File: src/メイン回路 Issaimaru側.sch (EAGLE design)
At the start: 3 parts

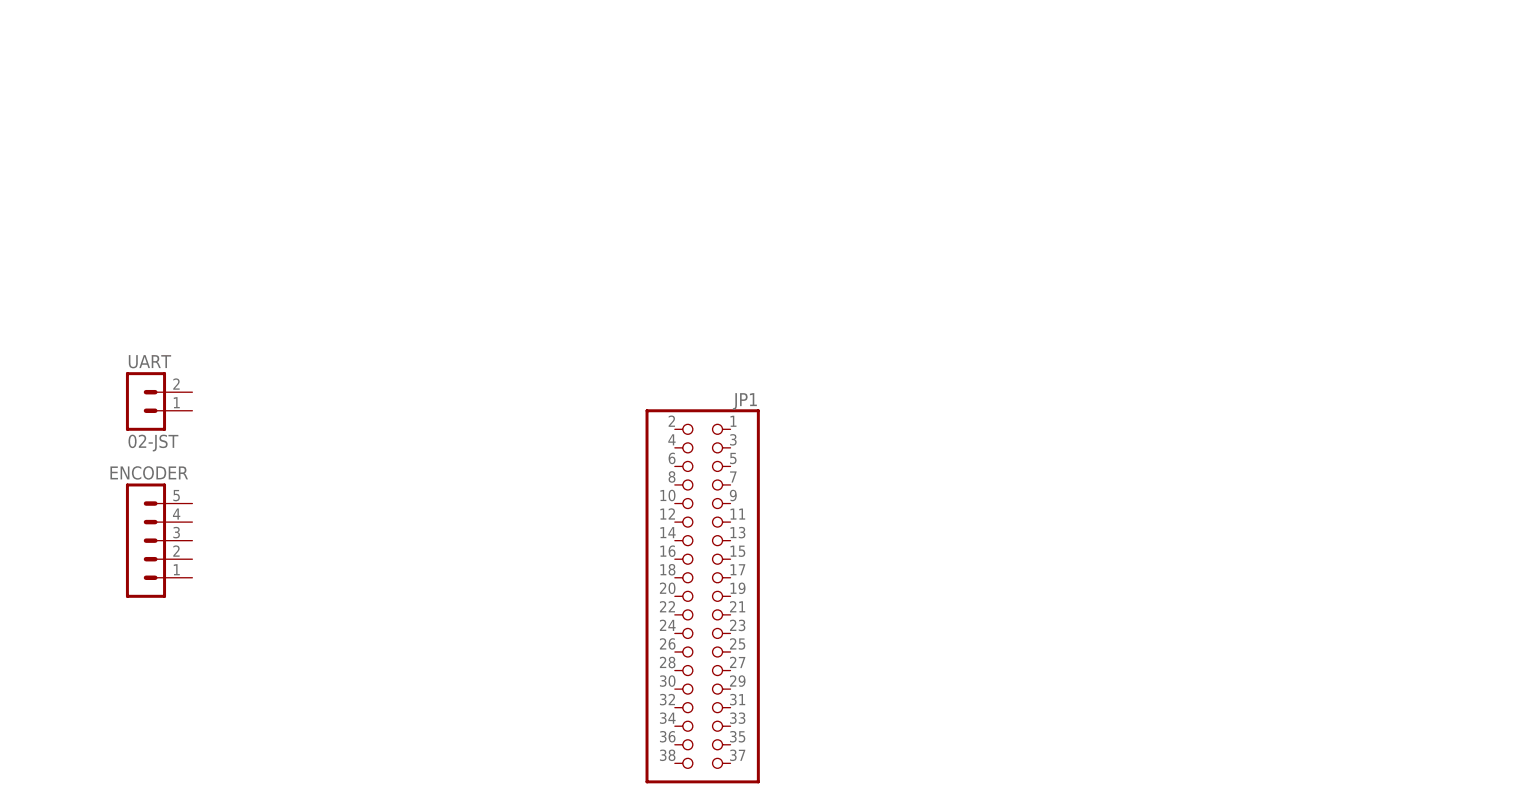
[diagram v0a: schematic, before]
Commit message: [add]コントローラー回路図の追加，メイン基板続き
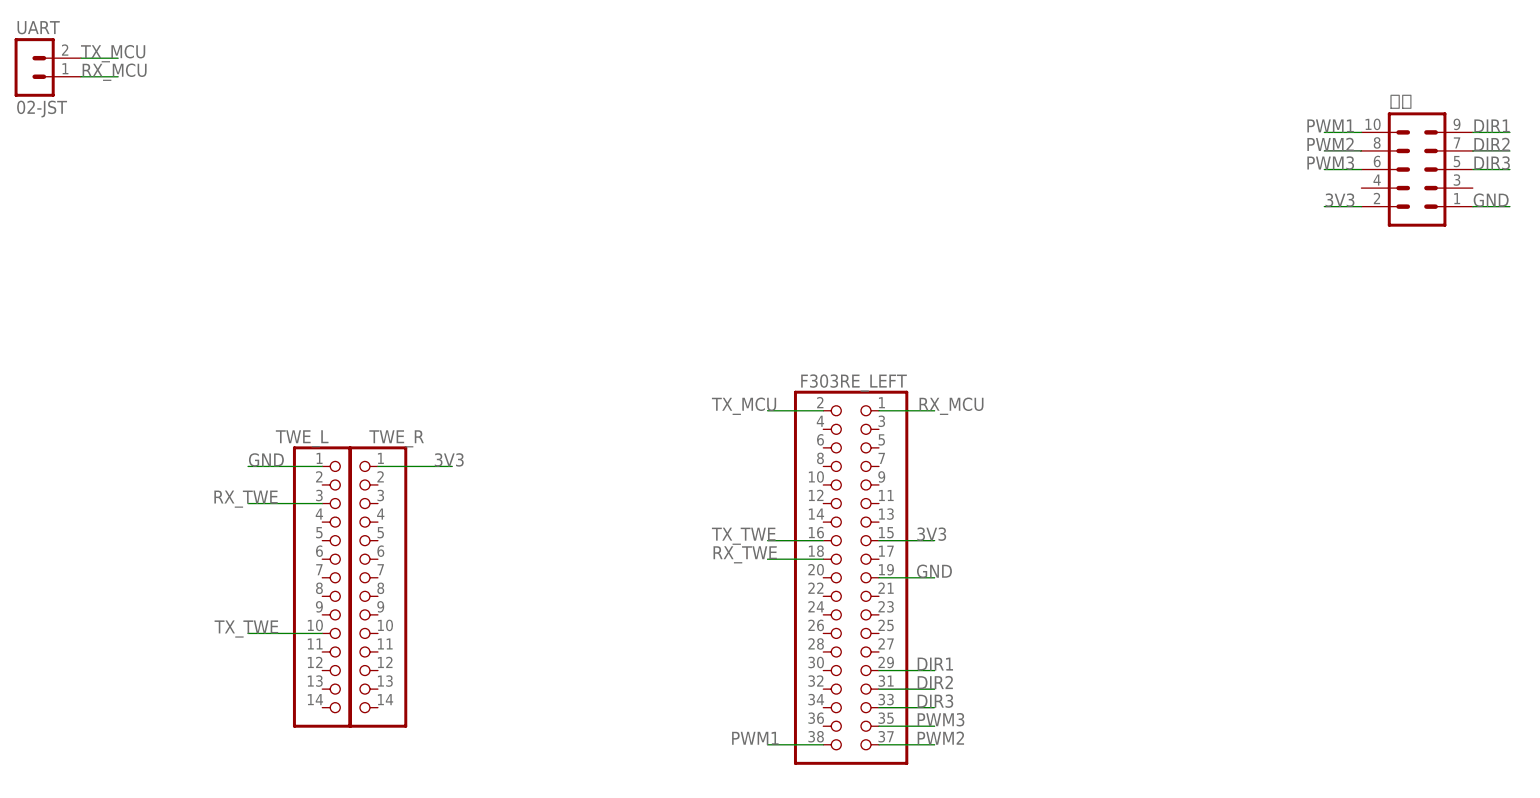
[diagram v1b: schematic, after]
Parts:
- removed ENCODER: (no value), con-jst-xh:05-JST
- removed JP1: (no value), pinhead:PINHD-2X19
- added F303RE_LEFT: (no value), pinhead:PINHD-2X19
- added TWE_L, TWE_R: (no value), pinhead:PINHD-1X14
- added 遠野: (no value), con-ml:ML10
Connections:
- new net 3V3: F303RE_LEFT.15, TWE_R.1, 遠野.2
- new net DIR1: F303RE_LEFT.29, 遠野.9
- new net DIR2: F303RE_LEFT.31, 遠野.7
- new net DIR3: F303RE_LEFT.33, 遠野.5
- new net GND: F303RE_LEFT.19, TWE_L.1, 遠野.1
- new net PWM1: F303RE_LEFT.38, 遠野.10
- new net PWM2: F303RE_LEFT.37, 遠野.8
- new net PWM3: F303RE_LEFT.35, 遠野.6
- new net RX_MCU: F303RE_LEFT.1, UART.1
- new net RX_TWE: F303RE_LEFT.18, TWE_L.3
- new net TX_MCU: F303RE_LEFT.2, UART.2
- new net TX_TWE: F303RE_LEFT.16, TWE_L.10
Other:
- moved on the sheet: UART
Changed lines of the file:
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@@
 </classes>
 <parts>
-<part name="JP1" library="pinhead" library_urn="urn:adsk.eagle:library:325" deviceset="PINHD-2X19" device="" package3d_urn="urn:adsk.eagle:package:22500/2"/>
+<part name="F303RE_LEFT" library="pinhead" library_urn="urn:adsk.eagle:library:325" deviceset="PINHD-2X19" device="" package3d_urn="urn:adsk.eagle:package:22500/2"/>
 <part name="FRAME1" library="frames" library_urn="urn:adsk.eagle:library:229" deviceset="A4L-LOC" device=""/>
 <part name="UART" library="con-jst-xh" deviceset="02-JST" device=""/>
-<part name="ENCODER" library="con-jst-xh" deviceset="05-JST" device=""/>
+<part name="TWE_L" library="pinhead" library_urn="urn:adsk.eagle:library:325" deviceset="PINHD-1X14" device="" package3d_urn="urn:adsk.eagle:package:22417/2"/>
+<part name="TWE_R" library="pinhead" library_urn="urn:adsk.eagle:library:325" deviceset="PINHD-1X14" device="" package3d_urn="urn:adsk.eagle:package:22417/2"/>
+<part name="遠野" library="con-ml" library_urn="urn:adsk.eagle:library:164" deviceset="ML10" device="" package3d_urn="urn:adsk.eagle:package:8676/1"/>
 </parts>
 <sheets>
@@
 </plain>
 <instances>
-<instance part="JP1" gate="G$1" x="119.38" y="86.36" smashed="yes" rot="MR0">
-<attribute name="NAME" x="125.73" y="109.855" size="1.778" layer="95" rot="MR0"/>
-<attribute name="VALUE" x="125.73" y="55.88" size="1.778" layer="96" rot="MR0"/>
+<instance part="F303RE_LEFT" gate="G$1" x="139.7" y="88.9" smashed="yes" rot="MR0">
+<attribute name="NAME" x="146.05" y="112.395" size="1.778" layer="95" rot="MR0"/>
+<attribute name="VALUE" x="146.05" y="58.42" size="1.778" layer="96" rot="MR0"/>
 </instance>
 <instance part="FRAME1" gate="G$1" x="0" y="0" smashed="yes">
@@
 <attribute name="SHEET" x="230.505" y="5.08" size="2.54" layer="94"/>
 </instance>
-<instance part="UART" gate="G$1" x="40.64" y="111.76" smashed="yes">
-<attribute name="VALUE" x="39.37" y="104.14" size="1.778" layer="96"/>
-<attribute name="NAME" x="39.37" y="115.062" size="1.778" layer="95"/>
+<instance part="UART" gate="G$1" x="25.4" y="157.48" smashed="yes">
+<attribute name="VALUE" x="24.13" y="149.86" size="1.778" layer="96"/>
+<attribute name="NAME" x="24.13" y="160.782" size="1.778" layer="95"/>
 </instance>
-<instance part="ENCODER" gate="G$1" x="40.64" y="91.44" smashed="yes">
-<attribute name="VALUE" x="39.37" y="81.28" size="1.778" layer="96"/>
-<attribute name="NAME" x="36.83" y="99.822" size="1.778" layer="95"/>
+<instance part="TWE_L" gate="A" x="68.58" y="86.36" smashed="yes">
+<attribute name="NAME" x="59.69" y="104.775" size="1.778" layer="95"/>
+<attribute name="VALUE" x="62.23" y="63.5" size="1.778" layer="96"/>
+</instance>
+<instance part="TWE_R" gate="A" x="71.12" y="86.36" smashed="yes" rot="MR0">
+<attribute name="NAME" x="80.01" y="104.775" size="1.778" layer="95" rot="MR0"/>
+<attribute name="VALUE" x="77.47" y="63.5" size="1.778" layer="96" rot="MR0"/>
+</instance>
+<instance part="遠野" gate="G$1" x="215.9" y="142.24" smashed="yes">
+<attribute name="VALUE" x="212.09" y="132.08" size="1.778" layer="96"/>
+<attribute name="NAME" x="212.09" y="150.622" size="1.778" layer="95"/>
 </instance>
 </instances>
@@
 </busses>
 <nets>
+<net name="TX_MCU" class="0">
+<segment>
+<pinref part="F303RE_LEFT" gate="G$1" pin="2"/>
+<wire x1="134.62" y1="109.22" x2="127" y2="109.22" width="0.1524" layer="91"/>
+<label x="119.38" y="109.22" size="1.778" layer="95"/>
+</segment>
+<segment>
+<pinref part="UART" gate="G$1" pin="2"/>
+<wire x1="33.02" y1="157.48" x2="38.1" y2="157.48" width="0.1524" layer="91"/>
+<label x="33.02" y="157.48" size="1.778" layer="95"/>
+</segment>
+</net>
+<net name="RX_MCU" class="0">
+<segment>
+<pinref part="F303RE_LEFT" gate="G$1" pin="1"/>
+<wire x1="142.24" y1="109.22" x2="149.86" y2="109.22" width="0.1524" layer="91"/>
+<label x="147.574" y="109.22" size="1.778" layer="95"/>
+</segment>
+<segment>
+<pinref part="UART" gate="G$1" pin="1"/>
+<wire x1="33.02" y1="154.94" x2="38.1" y2="154.94" width="0.1524" layer="91"/>
+<label x="33.02" y="154.94" size="1.778" layer="95"/>
+</segment>
+</net>
+<net name="GND" class="0">
+<segment>
+<pinref part="TWE_L" gate="A" pin="1"/>
+<wire x1="66.04" y1="101.6" x2="55.88" y2="101.6" width="0.1524" layer="91"/>
+<label x="55.88" y="101.6" size="1.778" layer="95"/>
+</segment>
+<segment>
+<pinref part="F303RE_LEFT" gate="G$1" pin="19"/>
+<wire x1="142.24" y1="86.36" x2="149.86" y2="86.36" width="0.1524" layer="91"/>
+<label x="147.32" y="86.36" size="1.778" layer="95"/>
+</segment>
+<segment>
+<pinref part="遠野" gate="G$1" pin="1"/>
+<wire x1="223.52" y1="137.16" x2="228.6" y2="137.16" width="0.1524" layer="91"/>
+<label x="223.52" y="137.16" size="1.778" layer="95"/>
+</segment>
+</net>
+<net name="3V3" class="0">
+<segment>
+<pinref part="TWE_R" gate="A" pin="1"/>
+<wire x1="73.66" y1="101.6" x2="83.82" y2="101.6" width="0.1524" layer="91"/>
+<label x="81.28" y="101.6" size="1.778" layer="95"/>
+</segment>
+<segment>
+<pinref part="F303RE_LEFT" gate="G$1" pin="15"/>
+<wire x1="142.24" y1="91.44" x2="149.86" y2="91.44" width="0.1524" layer="91"/>
+<label x="147.32" y="91.44" size="1.778" layer="95"/>
+</segment>
+<segment>
+<pinref part="遠野" gate="G$1" pin="2"/>
+<wire x1="208.28" y1="137.16" x2="203.2" y2="137.16" width="0.1524" layer="91"/>
+<label x="203.2" y="137.16" size="1.778" layer="95"/>
+</segment>
+</net>
+<net name="RX_TWE" class="0">
+<segment>
+<pinref part="TWE_L" gate="A" pin="3"/>
+<wire x1="66.04" y1="96.52" x2="55.88" y2="96.52" width="0.1524" layer="91"/>
+<label x="51.054" y="96.52" size="1.778" layer="95"/>
+</segment>
+<segment>
+<pinref part="F303RE_LEFT" gate="G$1" pin="18"/>
+<wire x1="134.62" y1="88.9" x2="127" y2="88.9" width="0.1524" layer="91"/>
+<label x="119.38" y="88.9" size="1.778" layer="95"/>
+</segment>
+</net>
+<net name="TX_TWE" class="0">
+<segment>
+<pinref part="TWE_L" gate="A" pin="10"/>
+<wire x1="66.04" y1="78.74" x2="55.88" y2="78.74" width="0.1524" layer="91"/>
+<label x="51.308" y="78.74" size="1.778" layer="95"/>
+</segment>
+<segment>
+<pinref part="F303RE_LEFT" gate="G$1" pin="16"/>
+<wire x1="134.62" y1="91.44" x2="127" y2="91.44" width="0.1524" layer="91"/>
+<label x="119.38" y="91.44" size="1.778" layer="95"/>
+</segment>
+</net>
+<net name="PWM1" class="0">
+<segment>
+<pinref part="遠野" gate="G$1" pin="10"/>
+<wire x1="208.28" y1="147.32" x2="203.2" y2="147.32" width="0.1524" layer="91"/>
+<label x="200.66" y="147.32" size="1.778" layer="95"/>
+</segment>
+<segment>
+<pinref part="F303RE_LEFT" gate="G$1" pin="38"/>
+<wire x1="134.62" y1="63.5" x2="127" y2="63.5" width="0.1524" layer="91"/>
+<label x="121.92" y="63.5" size="1.778" layer="95"/>
+</segment>
+</net>
+<net name="PWM2" class="0">
+<segment>
+<pinref part="遠野" gate="G$1" pin="8"/>
+<wire x1="208.28" y1="144.78" x2="203.2" y2="144.78" width="0.1524" layer="91"/>
+<label x="200.66" y="144.78" size="1.778" layer="95"/>
+</segment>
+<segment>
+<pinref part="F303RE_LEFT" gate="G$1" pin="37"/>
+<wire x1="142.24" y1="63.5" x2="149.86" y2="63.5" width="0.1524" layer="91"/>
+<label x="147.32" y="63.5" size="1.778" layer="95"/>
+</segment>
+</net>
+<net name="PWM3" class="0">
+<segment>
+<pinref part="遠野" gate="G$1" pin="6"/>
+<wire x1="208.28" y1="142.24" x2="203.2" y2="142.24" width="0.1524" layer="91"/>
+<label x="200.66" y="142.24" size="1.778" layer="95"/>
+</segment>
+<segment>
+<pinref part="F303RE_LEFT" gate="G$1" pin="35"/>
+<wire x1="142.24" y1="66.04" x2="149.86" y2="66.04" width="0.1524" layer="91"/>
+<label x="147.32" y="66.04" size="1.778" layer="95"/>
+</segment>
+</net>
+<net name="DIR3" class="0">
+<segment>
+<pinref part="遠野" gate="G$1" pin="5"/>
+<wire x1="223.52" y1="142.24" x2="228.6" y2="142.24" width="0.1524" layer="91"/>
+<label x="223.52" y="142.24" size="1.778" layer="95"/>
+</segment>
+<segment>
+<pinref part="F303RE_LEFT" gate="G$1" pin="33"/>
+<wire x1="142.24" y1="68.58" x2="149.86" y2="68.58" width="0.1524" layer="91"/>
+<label x="147.32" y="68.58" size="1.778" layer="95"/>
+</segment>
+</net>
+<net name="DIR2" class="0">
+<segment>
+<pinref part="遠野" gate="G$1" pin="7"/>
+<wire x1="223.52" y1="144.78" x2="228.6" y2="144.78" width="0.1524" layer="91"/>
+<label x="223.52" y="144.78" size="1.778" layer="95"/>
+</segment>
+<segment>
+<pinref part="F303RE_LEFT" gate="G$1" pin="31"/>
+<wire x1="142.24" y1="71.12" x2="149.86" y2="71.12" width="0.1524" layer="91"/>
+<label x="147.32" y="71.12" size="1.778" layer="95"/>
+</segment>
+</net>
+<net name="DIR1" class="0">
+<segment>
+<pinref part="遠野" gate="G$1" pin="9"/>
+<wire x1="223.52" y1="147.32" x2="228.6" y2="147.32" width="0.1524" layer="91"/>
+<label x="223.52" y="147.32" size="1.778" layer="95"/>
+</segment>
+<segment>
+<pinref part="F303RE_LEFT" gate="G$1" pin="29"/>
+<wire x1="142.24" y1="73.66" x2="149.86" y2="73.66" width="0.1524" layer="91"/>
+<label x="147.32" y="73.66" size="1.778" layer="95"/>
+</segment>
+</net>
 </nets>
 </sheet>
